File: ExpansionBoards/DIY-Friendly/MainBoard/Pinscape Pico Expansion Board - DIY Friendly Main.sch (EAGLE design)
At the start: 110 parts, among them IC1 UCC27524P, IC10 ULN2803A, IC11 SN74HC165N, IC12 SN74HC165N, IC13 SN74HC74NE4, IC14 PC827, IC15 S-80833CLY, IC16 SN74HC165N, IC18 SN74HC165N, IC2 UCC27524P, IC3 UCC27524P, IC4 UCC27524P, IC5 UCC27524P, IC6 UCC27524P, IC7 ULN2803A, IC8 ULN2803A, IC9 ULN2803A, J1 30316-6002HB, J10 215079-4, J11 640454-2, J13 640445-2, J2 640445-4, J3 640445-5, J4 640445-9, J5 1-640456-0, J6 1-640456-0, J7 1-640456-0, J8 1-640456-0, J9 30308-6002HB, Q1 FDPF085N10A, Q10 FDPF085N10A, Q11 FDPF085N10A, Q12 FDPF085N10A, Q13 BC337-25, Q15 2N5195G, Q16 2N2222A, Q2 FDPF085N10A, Q3 FDPF085N10A, Q4 FDPF085N10A, Q5 FDPF085N10A, Q6 FDPF085N10A, Q7 FDPF085N10A, Q8 FDPF085N10A, Q9 FDPF085N10A

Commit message: expansion board improvements
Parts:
- J2: value 640445-4 -> 640445-6; device SamacSys_Parts:640445-4 -> SamacSys_Parts:640445-6
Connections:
- net 12V: now also J2.5; no longer J2.3
- net 5V: now also J2.6; no longer J2.4
- net GND: now also J2.3, J2.4
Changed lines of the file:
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@@
 <attribute name="PARTNO" value="810-FG14X5R1H475KRT0"/>
 </part>
-<part name="J2" library="SamacSys_Parts" deviceset="640445-4" device=""/>
 <part name="GND38" library="supply1" deviceset="GND" device=""/>
 <part name="J11" library="SamacSys_Parts" deviceset="640454-2" device=""/>
@@
 <attribute name="PARTNO" value="660-MFS1/4DCT52R47R0"/>
 </part>
+<part name="J2" library="SamacSys_Parts" deviceset="640445-6" device=""/>
 </parts>
 <sheets>
@@
 <instance part="D1" gate="G$1" x="119.38" y="68.58"/>
 <instance part="J12" gate="A" x="198.12" y="96.52"/>
-<instance part="J2" gate="G$1" x="185.42" y="170.18" smashed="yes">
-<attribute name="NAME" x="201.93" y="172.72" size="1.778" layer="95" align="center-left"/>
-<attribute name="VALUE" x="201.93" y="170.18" size="1.778" layer="96" align="center-left"/>
-</instance>
 <instance part="J14" gate="A" x="198.12" y="134.62"/>
 <instance part="R26" gate="G$1" x="276.86" y="38.1" smashed="yes" rot="MR180">
@@
 <attribute name="NAME" x="297.942" y="39.37" size="1.778" layer="95" rot="MR180" align="center-left"/>
 <attribute name="VALUE" x="297.942" y="36.83" size="1.778" layer="96" rot="MR180" align="center-left"/>
+</instance>
+<instance part="J2" gate="G$1" x="185.42" y="170.18" smashed="yes">
+<attribute name="NAME" x="201.93" y="170.18" size="1.778" layer="95" align="center-left"/>
+<attribute name="VALUE" x="201.93" y="167.64" size="1.778" layer="96" align="center-left"/>
 </instance>
 </instances>
@@
 </segment>
 <segment>
-<pinref part="J2" gate="G$1" pin="2"/>
 <wire x1="182.88" y1="167.64" x2="185.42" y2="167.64" width="0.1524" layer="91"/>
-<pinref part="J2" gate="G$1" pin="1"/>
 <wire x1="180.34" y1="170.18" x2="182.88" y2="170.18" width="0.1524" layer="91"/>
 <label x="180.34" y="170.18" size="1.27" layer="95" rot="R180" xref="yes"/>
@@
 <wire x1="182.88" y1="167.64" x2="182.88" y2="170.18" width="0.1524" layer="91"/>
 <junction x="182.88" y="170.18"/>
+<wire x1="182.88" y1="167.64" x2="182.88" y2="165.1" width="0.1524" layer="91"/>
+<junction x="182.88" y="167.64"/>
+<wire x1="182.88" y1="165.1" x2="185.42" y2="165.1" width="0.1524" layer="91"/>
+<pinref part="J2" gate="G$1" pin="1"/>
+<pinref part="J2" gate="G$1" pin="2"/>
+<pinref part="J2" gate="G$1" pin="3"/>
+<wire x1="182.88" y1="165.1" x2="182.88" y2="162.56" width="0.1524" layer="91"/>
+<junction x="182.88" y="165.1"/>
+<pinref part="J2" gate="G$1" pin="4"/>
+<wire x1="182.88" y1="162.56" x2="185.42" y2="162.56" width="0.1524" layer="91"/>
 </segment>
 <segment>
@@
 <net name="5V" class="0">
 <segment>
-<pinref part="J2" gate="G$1" pin="4"/>
-<wire x1="182.88" y1="162.56" x2="185.42" y2="162.56" width="0.1524" layer="91"/>
-<label x="182.88" y="162.56" size="1.27" layer="95" rot="R180" xref="yes"/>
+<label x="182.88" y="157.48" size="1.27" layer="95" rot="R180" xref="yes"/>
+<pinref part="J2" gate="G$1" pin="6"/>
+<wire x1="185.42" y1="157.48" x2="182.88" y2="157.48" width="0.1524" layer="91"/>
 </segment>
 </net>
 <net name="12V" class="0">
 <segment>
-<pinref part="J2" gate="G$1" pin="3"/>
-<label x="182.88" y="165.1" size="1.27" layer="95" rot="R180" xref="yes"/>
-<wire x1="182.88" y1="165.1" x2="185.42" y2="165.1" width="0.1524" layer="91"/>
-</segment>
-</net>
+<label x="182.88" y="160.02" size="1.27" layer="95" rot="R180" xref="yes"/>
+<pinref part="J2" gate="G$1" pin="5"/>
+<wire x1="185.42" y1="160.02" x2="182.88" y2="160.02" width="0.1524" layer="91"/>
+</segment>
+</net>

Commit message: minor board updates
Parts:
- R26, R28, R32, R33: device resistor:R-US_0204/5 -> resistor:R-US_0204/7
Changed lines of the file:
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@@
 <part name="R24" library="SamacSys_Parts - backup" deviceset="4609X-101-122LF" device="" value="4609X-101-103F"/>
 <part name="R25" library="SamacSys_Parts - backup" deviceset="4609X-101-122LF" device="" value="4609X-101-103F"/>
-<part name="R26" library="resistor" deviceset="R-US_" device="0204/5" value="1K">
+<part name="R26" library="resistor" deviceset="R-US_" device="0204/7" value="1K">
 <attribute name="PARTNO" value="660-MFS1/4DCT52R47R0"/>
 </part>
-<part name="R28" library="resistor" deviceset="R-US_" device="0204/5" value="22K">
+<part name="R28" library="resistor" deviceset="R-US_" device="0204/7" value="22K">
 <attribute name="PARTNO" value="660-MFS1/4DCT52R47R0"/>
 </part>
 <part name="Q16" library="SamacSys_Parts" deviceset="2N2222A" device=""/>
-<part name="R32" library="resistor" deviceset="R-US_" device="0204/5" value="10K">
+<part name="R32" library="resistor" deviceset="R-US_" device="0204/7" value="10K">
 <attribute name="PARTNO" value="660-MFS1/4DCT52R47R0"/>
 </part>
 <part name="GND2" library="supply1" deviceset="GND" device=""/>
 <part name="GND3" library="supply1" deviceset="GND" device=""/>
-<part name="R33" library="resistor" deviceset="R-US_" device="0204/5" value="2.2k">
+<part name="R33" library="resistor" deviceset="R-US_" device="0204/7" value="2.2k">
 <attribute name="PARTNO" value="660-MFS1/4DCT52R47R0"/>
 </part>

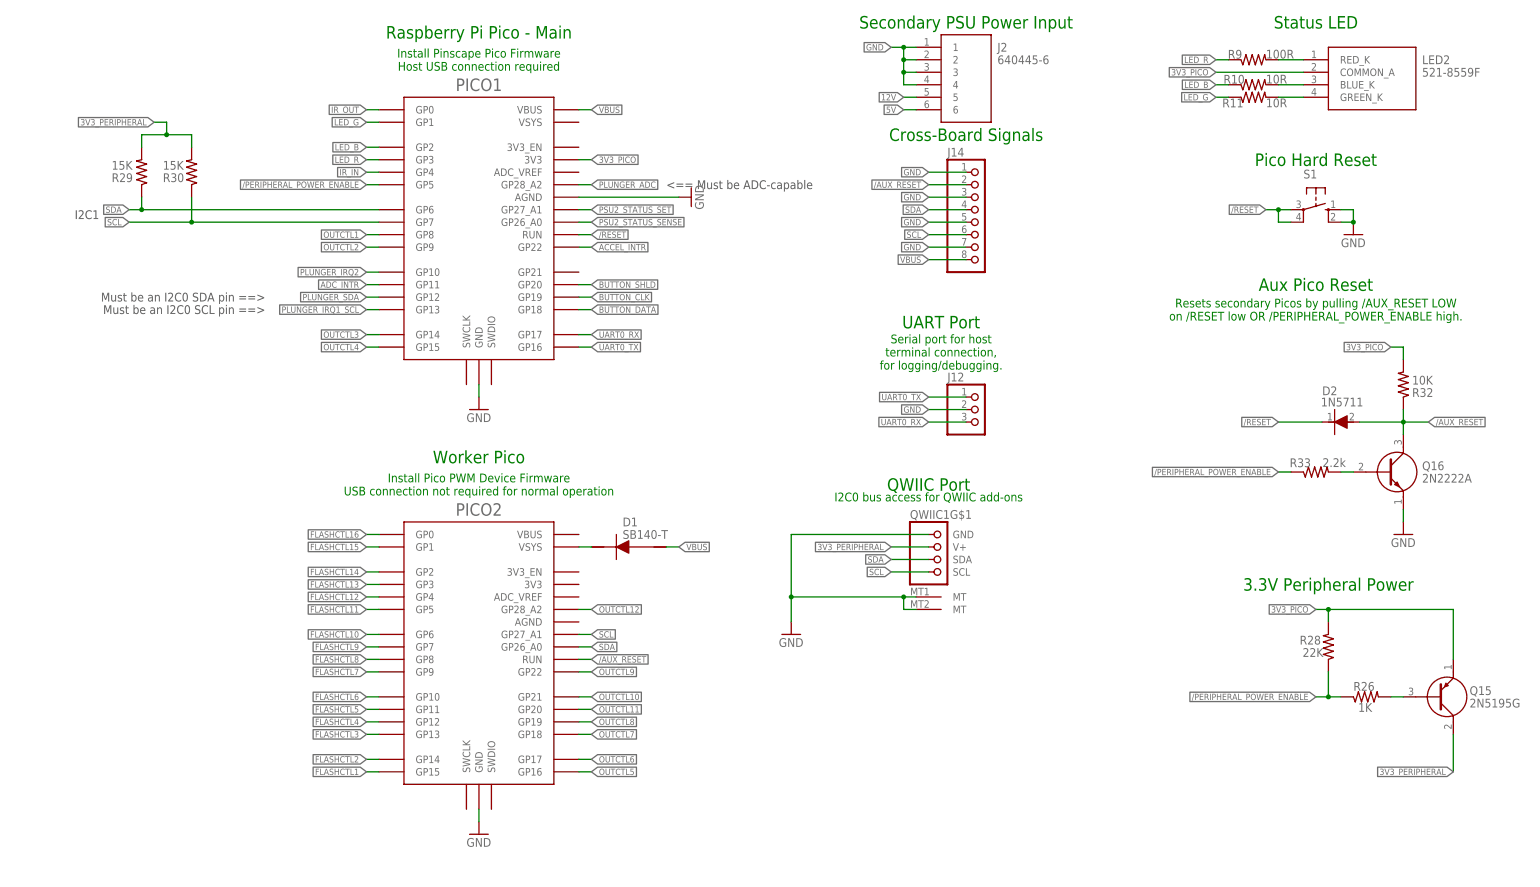
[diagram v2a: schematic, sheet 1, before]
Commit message: Remove pull-up to primary Pico 3V3 on aux Pico reset
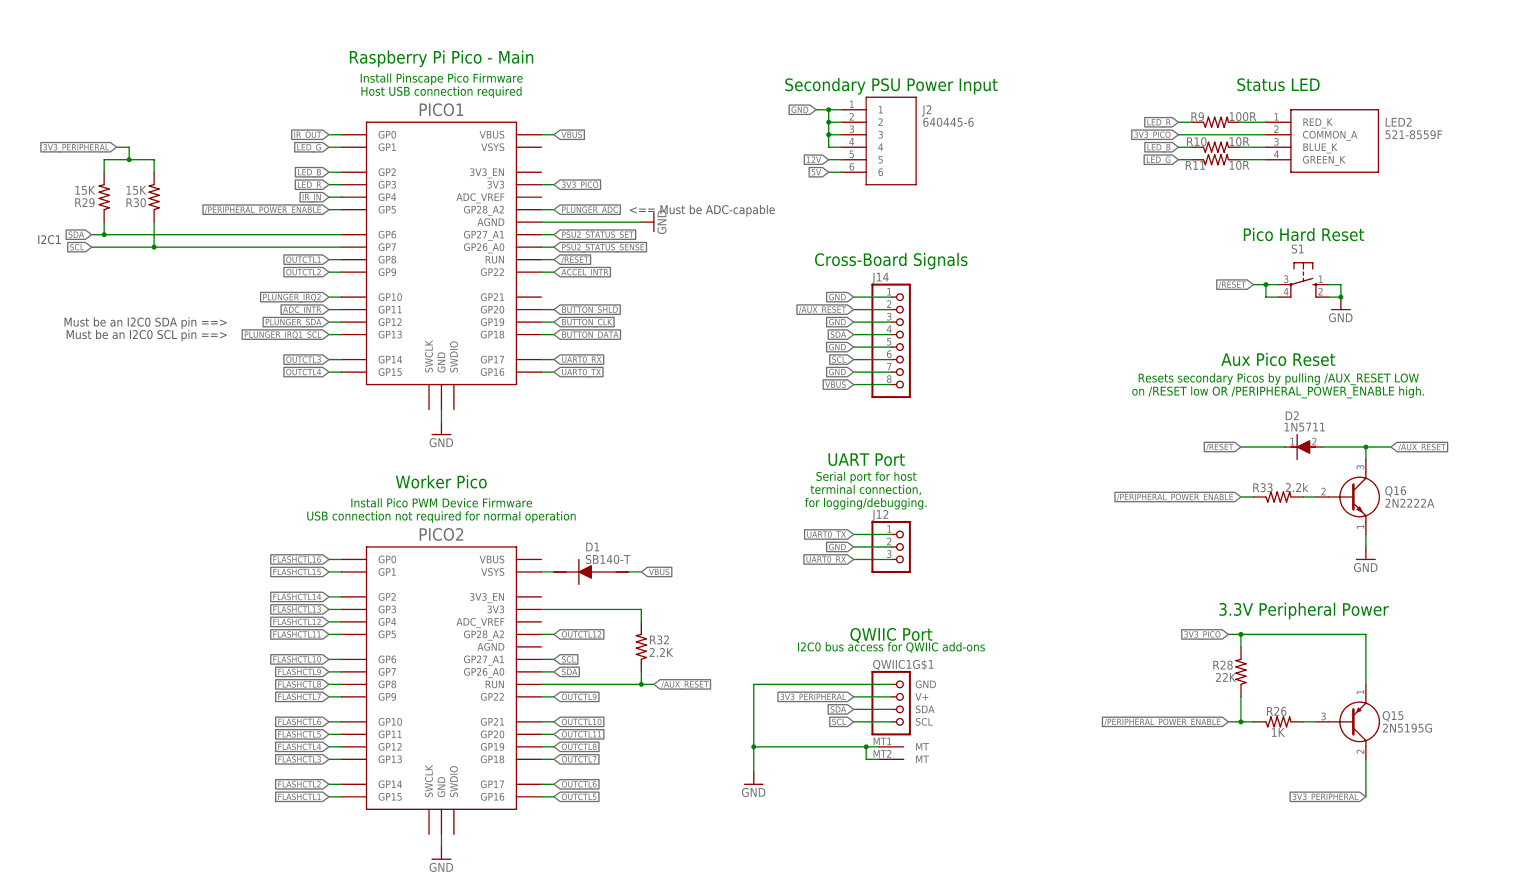
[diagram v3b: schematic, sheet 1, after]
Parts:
- R32: value 10K -> 2.2K
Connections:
- new net N$34: PICO2.3V3, R32.2
- net 3V3_PICO: no longer R32.2
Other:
- moved on the sheet: D1, D2, J12, J14, J2, LED2, PICO1, PICO2, Q15, Q16, QWIIC1G$1, R10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

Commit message: DIY board: individual reset buttons per Pico; swap cross-board connectors
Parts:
- removed D2: 1N5711, SamacSys_Parts:1N5711
- added R34: 4.7K, resistor:R-US_0204/7
- added S2: (no value), switch-omron:10-XX
- J14: value (none) -> SSQ-108-02-T-S-RA; device pinhead:PINHD-1X8/90 -> SamacSys_Parts:SSQ-108-02-T-S-RA
- R29, R30: device resistor:R-US_0204/5 -> resistor:R-US_0204/7
- R32: value 2.2K -> 4.7K
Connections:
- removed net /AUX_RESET: D2.A, J14.2, PICO2.RUN, Q16.C, R32.1
- removed net /RESET: D2.K, PICO1.RUN, S1.P, S1.P1
- new net N$35: PICO2.RUN, Q16.C, R32.1, S2.P, S2.P1
- new net N$36: PICO1.RUN, R34.1, S1.P, S1.P1
- net /PERIPHERAL_POWER_ENABLE: now also J14.7
- net 3V3_PICO: now also R34.2
- net GND: now also J14.2, J14.4, J14.6, J14.8, S2.S, S2.S1; no longer J14.1, J14.3, J14.5, J14.7
- net SCL: now also J14.3; no longer J14.6
- net SDA: now also J14.5; no longer J14.4
- net VBUS: now also J14.1; no longer J14.8
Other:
- note added: "Aux Pico is powered from primary Pico USB bus power. Diode prevents back-flow when aux Pico USB is plugged in - see Pico Data Sheet > "Powering Pico"."
- note added: "Main Pico Hard Reset"
- note added: "Power In"
- note added: "Resets secondary Pico when main Pico drives /PERIPHERAL_POWER_ENABLE high, or manually via button."
- note added: "Software-controlled switch for 3V3 power to accelerometer & ADC, to allow power-cycle reset under software control."
- note added: "Worker Pico 0"
- note removed: "Pico Hard Reset"
- note removed: "Resets secondary Picos by pulling /AUX_RESET LOW on /RESET low OR /PERIPHERAL_POWER_ENABLE high."
- note removed: "Worker Pico"
